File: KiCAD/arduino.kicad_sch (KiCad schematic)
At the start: 1 part, among them U2 Metro_ESP32S3

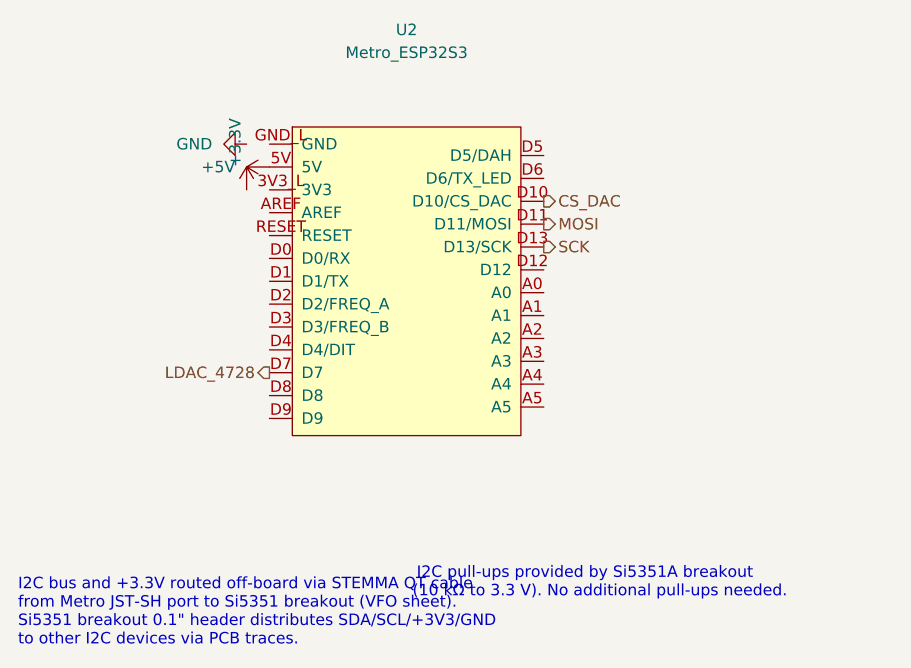
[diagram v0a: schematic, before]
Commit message: kicad(bias): build complete grid-bias sheet (Design A: dual OPA454)
New sheet untitled.kicad_sch (sheet name "Bias", file to be renamed
bias.kicad_sch) implementing the OPA454 high-voltage design per the
Grid_Bias_Schematic.pdf design doc:

- LM7805 (U9) generates the +5 V supply rail from +12 V (~30 mA load,
  no heatsink needed at ~270 mW dissipation)
- LM4040DIZ-5.0 (U11) generates a SEPARATE +5 V_REF precision reference
  biased from +12 V via R_Z = 2.2 kΩ; cathode bypassed by C23 (100 nF).
  Drives only R_GA / R_GB (the two OPA454 summing-junction inputs) and
  the cathode-monitor's 1.5 V threshold divider on its own sheet
- Two OPA454 channels (U5 = Tube A, U10 = Tube B) each with R_F = 170 k,
  R_G = 10 k, R_GL = 22 k, R_pad = 1 k, plus 2N7000 bias-slam (Q2, Q3)
  sharing one R_GATE = 10 k. Transfer function V_out = 18·V_DAC - 85
- Shared bypass caps across U5/U10 V+ and V- rails (1 µF X7R bulk +
  100 nF HF on each rail); justified by grid-bias bandwidth being
  effectively DC vs textbook µV-class instrumentation recommendation

Supporting changes:

- New xmitter:OPA454 multi-unit symbol (Unit A = 3-pin op-amp triangle
  with IN-, IN+, OUT; Unit B = 5-pin power/enable block with V+, V-,
  ED, EDCOMM, STATFLG). Built via tools/add_opa454_symbol.py
- xmitter_prj/grid_bias.sch: V2 = 90 V (was 85), V3 = 5 V (was 12) to
  match the PDF design's +5 V / -90 V supply rails; LM4040 stays at 5 V
- pa_cathode_monitor.md: switch comparator V_REF from the bogus
  LM4040DIZ-1.2 (doesn't exist - LM4040 minimum is 2.048 V) to a shared
  LM4040DIZ-5.0 with a 4.7 k / 1 k trim / 1.5 k divider giving 1.5 V
  nominal (1.21 V to 1.74 V across full pot)
- Documentation/grid_bias.md: full subsystem design doc covering
  architecture decisions, transfer function, per-channel topology, BOM,
  inter-sheet I/O, calibration procedure, and open items
- Documentation/kicad_custom_symbols.md: OPA454 entry plus a note on
  the KiCad sub-symbol naming gotcha (NAME_{unit}_{body_style}, not th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
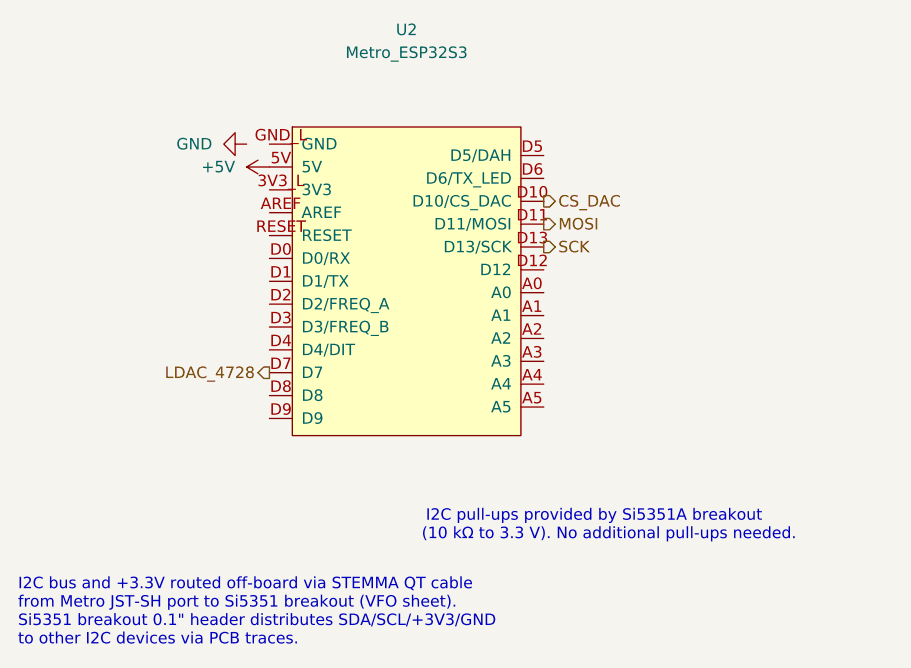
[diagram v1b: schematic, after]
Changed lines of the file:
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@@
 	(generator_version "10.0")
 	(paper "A4")
+	(text "I2C bus and +3.3V routed off-board via STEMMA QT cable\nfrom Metro JST-SH port to Si5351 breakout (VFO sheet).\nSi5351 breakout 0.1\" header distributes SDA/SCL/+3V3/GND\nto other I2C devices via PCB traces."
+		(exclude_from_sim no)
+		(at 60.96 110.49 0)
+		(effects
+			(font
+				(size 1.27 1.27)
+			)
+			(justify left)
+		)
+	)
 	(text "I2C pull-ups provided by Si5351A breakout\n      (10 kΩ to 3.3 V). No additional pull-ups needed."
 		(exclude_from_sim no)
-		(at 123.952 107.188 0)
+		(at 124.968 100.838 0)
 		(effects
 			(font
@@
 		)
 	)
-	(symbol
-		(lib_id "power:+3.3V")
-		(at 86.36 63.5 0)
-		(unit 1)
-		(body_style 1)
-		(exclude_from_sim no)
-		(in_bom yes)
-		(on_board yes)
-		(in_pos_files yes)
-		(dnp no)
-		(fields_autoplaced yes)
-		(property "Reference" "#PWR031"
-			(at 92.71 60.96 0)
-			(hide yes)
-			(show_name no)
-			(do_not_autoplace no)
-			(effects
-				(font
-					(size 1.27 1.27)
-				)
-			)
-		)
-		(property "Value" "+3.3V"
-			(at 85.09 60.9599 90)
-			(show_name no)
-			(do_not_autoplace no)
-			(effects
-				(font
-					(size 1.27 1.27)
-				)
-				(justify left)
-			)
-		)
-		(property "Footprint" ""
-			(at 88.9 60.96 0)
-			(hide yes)
-			(show_name no)
-			(do_not_autoplace no)
-			(effects
-				(font
-					(size 1.27 1.27)
-				)
-			)
-		)
-		(property "Datasheet" ""
-			(at 88.9 60.96 0)
-			(hide yes)
-			(show_name no)
-			(do_not_autoplace no)
-			(effects
-				(font
-					(size 1.27 1.27)
-				)
-			)
-		)
-		(property "Description" "Power symbol creates a global label with name \"+5V\""
-			(at 88.9 60.96 0)
-			(hide yes)
-			(show_name no)
-			(do_not_autoplace no)
-			(effects
-				(font
-					(size 1.27 1.27)
-				)
-			)
-		)
-		(pin "1"
-		)
-		(instances
-			(project "KiCAD"
-				(path "/d3de40b8-856b-4fbd-829c-f45ffcd55742/2d83d0b5-86d4-4ced-ab68-6465e3dc2d72"
-					(reference "#PWR030")
-					(unit 1)
-				)
-			)
-		)
-	)
-	(text "I2C bus and +3.3V routed off-board via STEMMA QT cable\nfrom Metro JST-SH port to Si5351 breakout (VFO sheet).\nSi5351 breakout 0.1\" header distributes SDA/SCL/+3V3/GND\nto other I2C devices via PCB traces."
-		(exclude_from_sim no)
-		(at 60.96 110.49 0)
-		(effects
-			(font
-				(size 1.27 1.27)
-			)
-			(justify left)
-		)
-	)
